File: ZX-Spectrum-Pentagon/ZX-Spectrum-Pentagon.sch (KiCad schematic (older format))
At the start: 0 parts

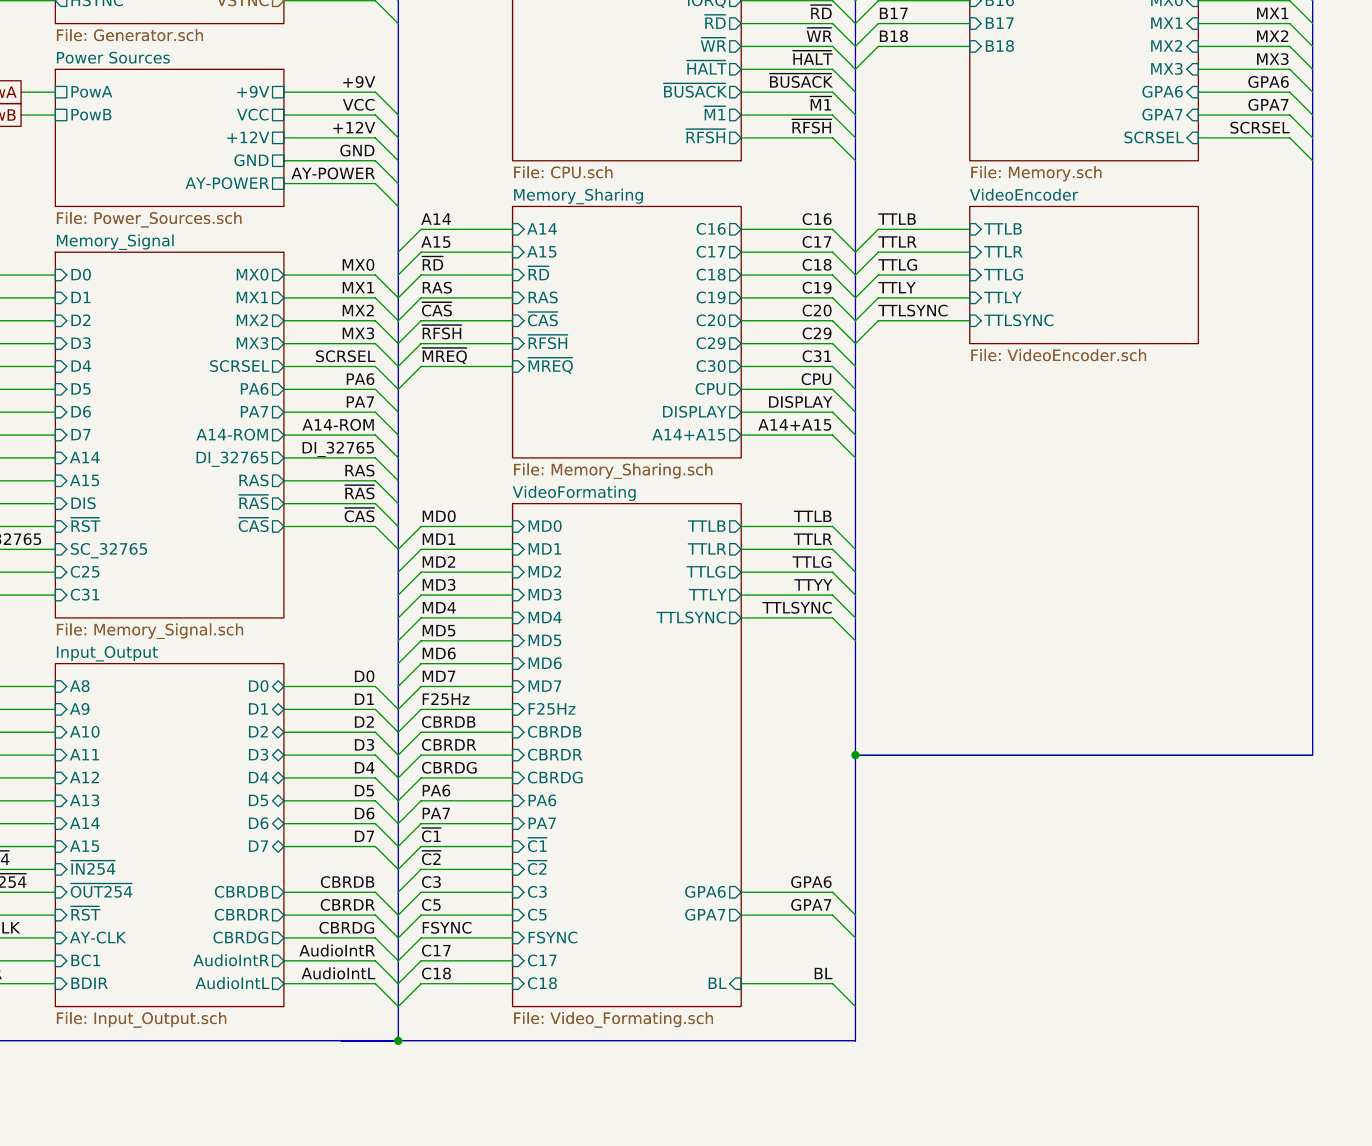
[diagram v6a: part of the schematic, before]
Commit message: improve VideoEncoder
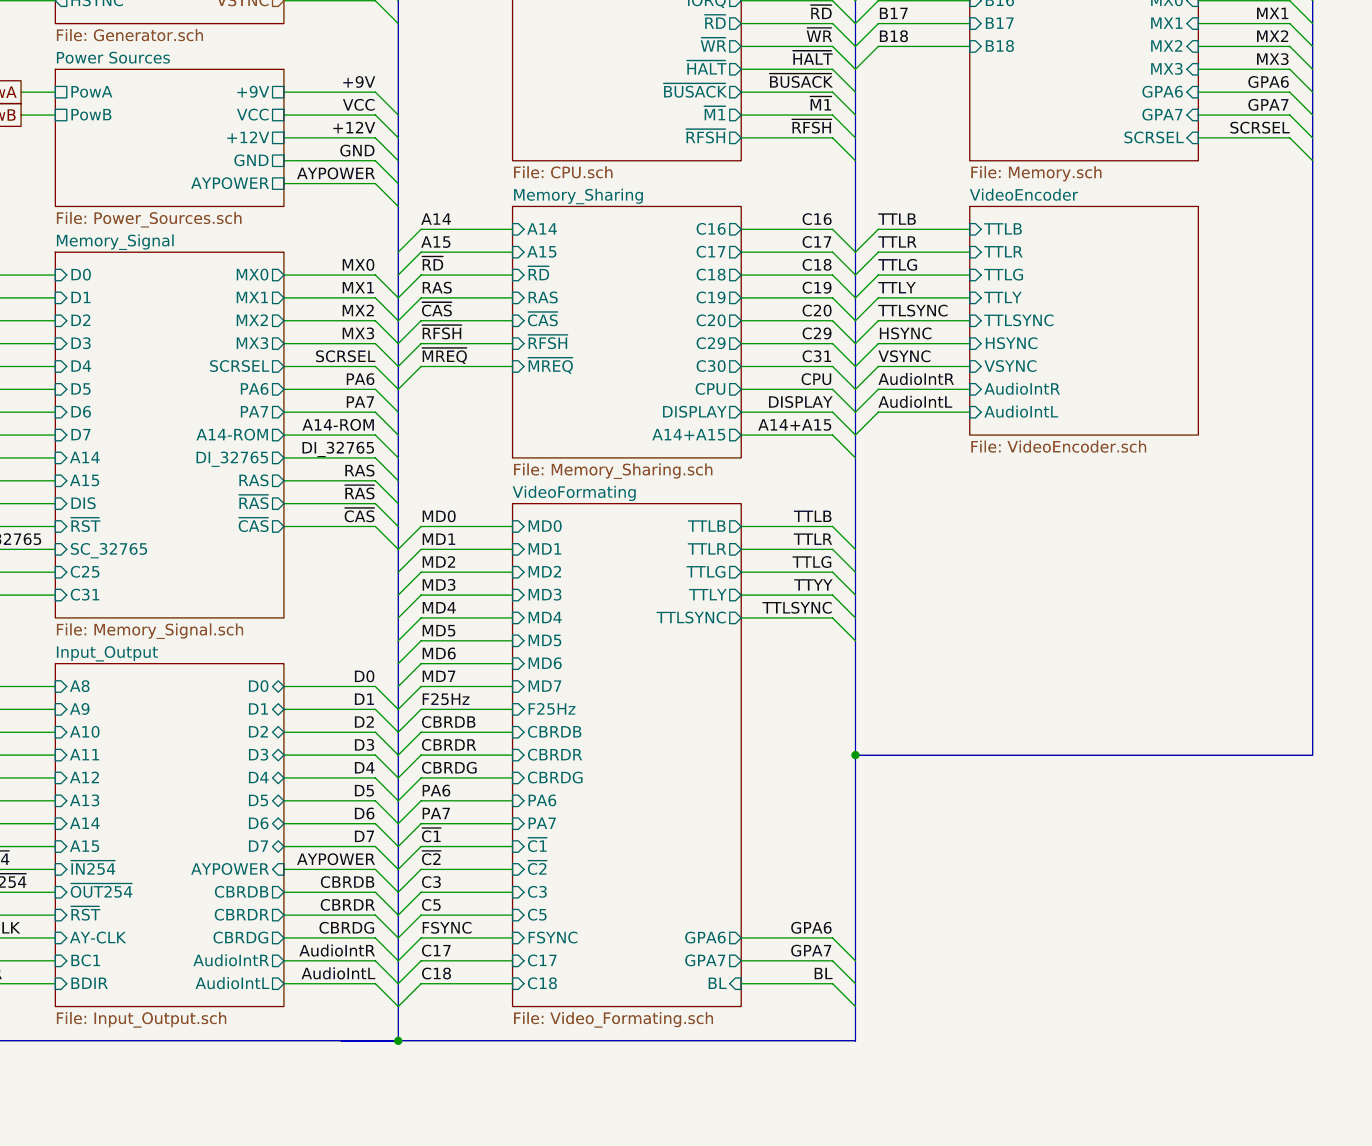
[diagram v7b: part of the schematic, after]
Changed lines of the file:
@@
 F6 "+12V" U R 2500 3800 50
 F7 "GND" U R 2500 3900 50
-F8 "AY-POWER" U R 2500 4000 50
+F8 "AYPOWER" U R 2500 4000 50
 $EndSheet
 Text Label 2900 2900 2    50   ~ 0
@@
 $EndSheet
 Text Label 2900 4000 2    50   ~ 0
-AY-POWER
+AYPOWER
 Wire Wire Line
 	2500 4000 2900 4000
@@
 F24 "PA7" I L 3500 6800 50
 F25 "C5" I L 3500 7200 50
-F26 "GPA6" O R 4500 7100 50
-F27 "GPA7" O R 4500 7200 50
+F26 "GPA6" O R 4500 7300 50
+F27 "GPA7" O R 4500 7400 50
 F28 "FSYNC" I L 3500 7300 50
 F29 "TTLY" O R 4500 5800 50
@@
 C5
 Entry Wire Line
-	4900 7100 5000 7200
-Entry Wire Line
-	4900 7200 5000 7300
-Wire Wire Line
-	4500 7100 4900 7100
-Wire Wire Line
-	4500 7200 4900 7200
-Text Label 4900 7100 2    50   ~ 0
+	4900 7300 5000 7400
+Entry Wire Line
+	4900 7400 5000 7500
+Wire Wire Line
+	4500 7300 4900 7300
+Wire Wire Line
+	4500 7400 4900 7400
+Text Label 4900 7300 2    50   ~ 0
 GPA6
-Text Label 4900 7200 2    50   ~ 0
+Text Label 4900 7400 2    50   ~ 0
 GPA7
 Entry Wire Line
@@
 F27 "AudioIntR" O R 2500 7400 50
 F28 "AudioIntL" O R 2500 7500 50
+F29 "AYPOWER" I R 2500 7000 50
 $EndSheet
 Text HLabel 2500 3200 0    50   Input ~ 0
@@
 NoConn ~ 17200 9450
 $Sheet
-S 5500 4100 1000 600
+S 5500 4100 1000 1000
 U 62BF0F7B
 F0 "VideoEncoder" 50
@@
 F5 "TTLY" I L 5500 4500 50
 F6 "TTLSYNC" I L 5500 4600 50
+F7 "HSYNC" I L 5500 4700 50
+F8 "VSYNC" I L 5500 4800 50
+F9 "AudioIntR" I L 5500 4900 50
+F10 "AudioIntL" I L 5500 5000 50
 $EndSheet
 Entry Wire Line
@@
 Text Label 4900 5900 2    50   ~ 0
 TTLSYNC
+Entry Wire Line
+	5000 4800 5100 4700
+Entry Wire Line
+	5000 4900 5100 4800
+Wire Wire Line
+	5100 4700 5500 4700
+Wire Wire Line
+	5100 4800 5500 4800
+Text Label 5100 4700 0    50   ~ 0
+HSYNC
+Text Label 5100 4800 0    50   ~ 0
+VSYNC
+Entry Wire Line
+	2900 7000 3000 7100
+Wire Wire Line
+	2500 7000 2900 7000
+Text Label 2900 7000 2    50   ~ 0
+AYPOWER
+Entry Wire Line
+	5000 5000 5100 4900
+Entry Wire Line
+	5000 5100 5100 5000
+Wire Wire Line
+	5100 4900 5500 4900
+Wire Wire Line
+	5100 5000 5500 5000
+Text Label 5100 4900 0    50   ~ 0
+AudioIntR
+Text Label 5100 5000 0    50   ~ 0
+AudioIntL
 Wire Bus Line
 	5000 6500 5000 7750
